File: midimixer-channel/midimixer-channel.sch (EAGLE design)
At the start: 115 parts, among them IC1 74LS595D, IC2 74LS595D, IC3 74LS595D, IC4 74165D, IC5 74165D, U1 LM1117IMPX-3.3/NOPB

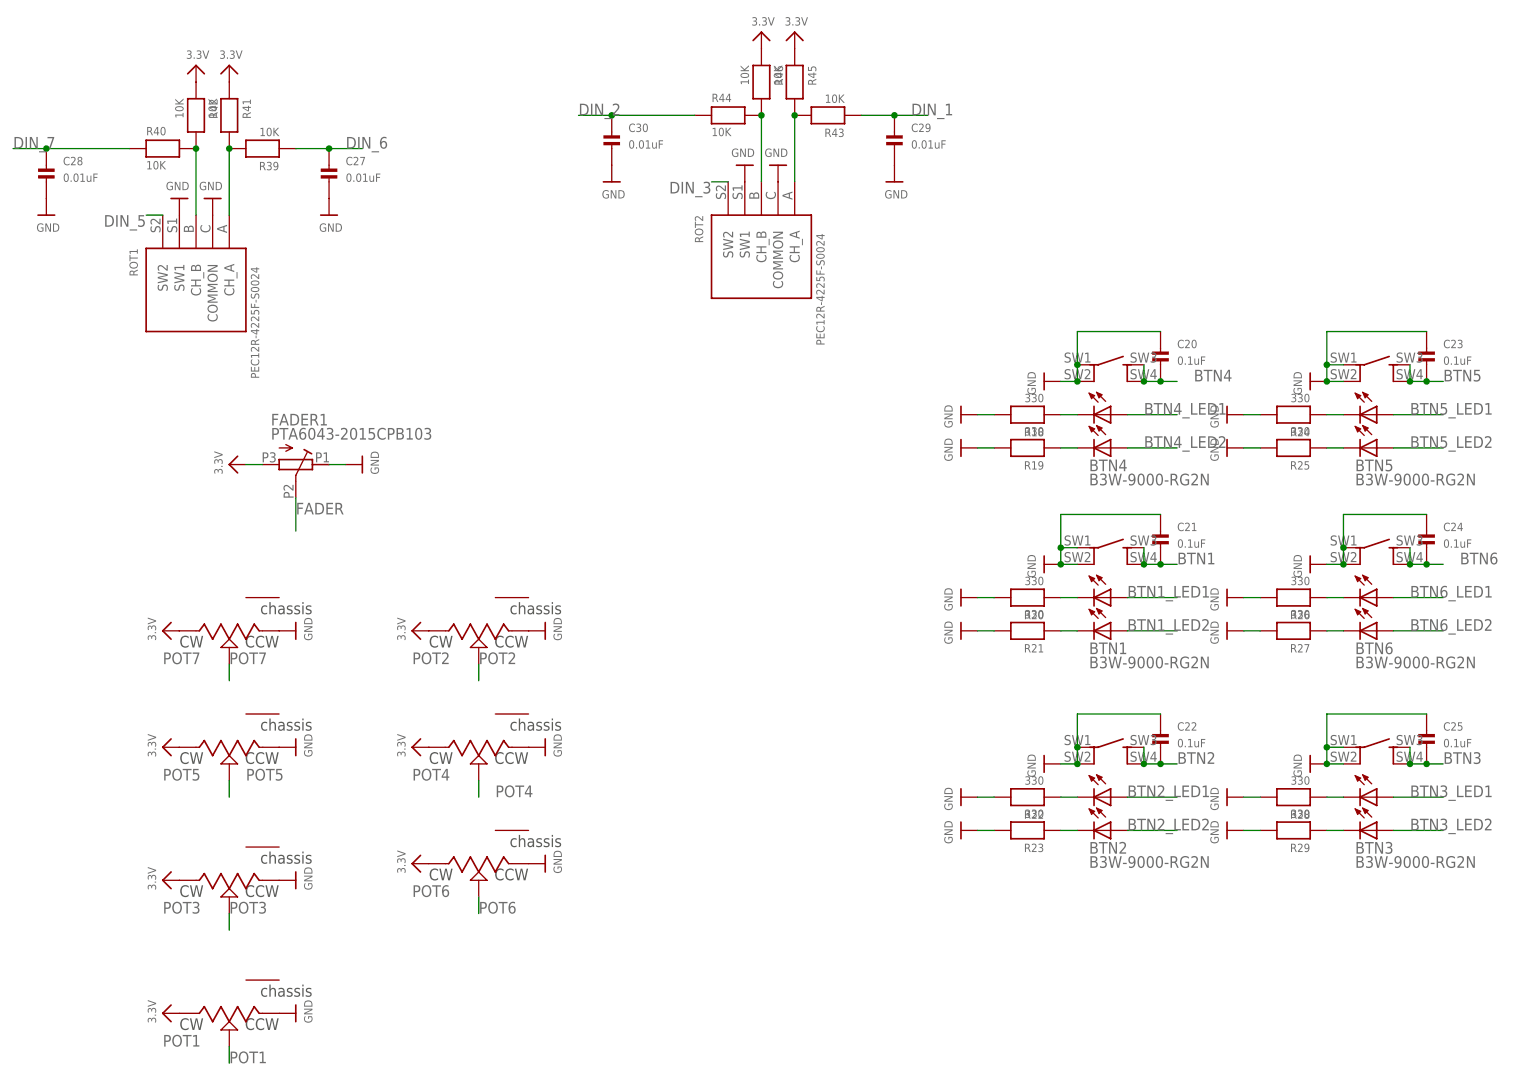
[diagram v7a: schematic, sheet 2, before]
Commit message: midimixer-channel: change green led resistors, some other misc changes
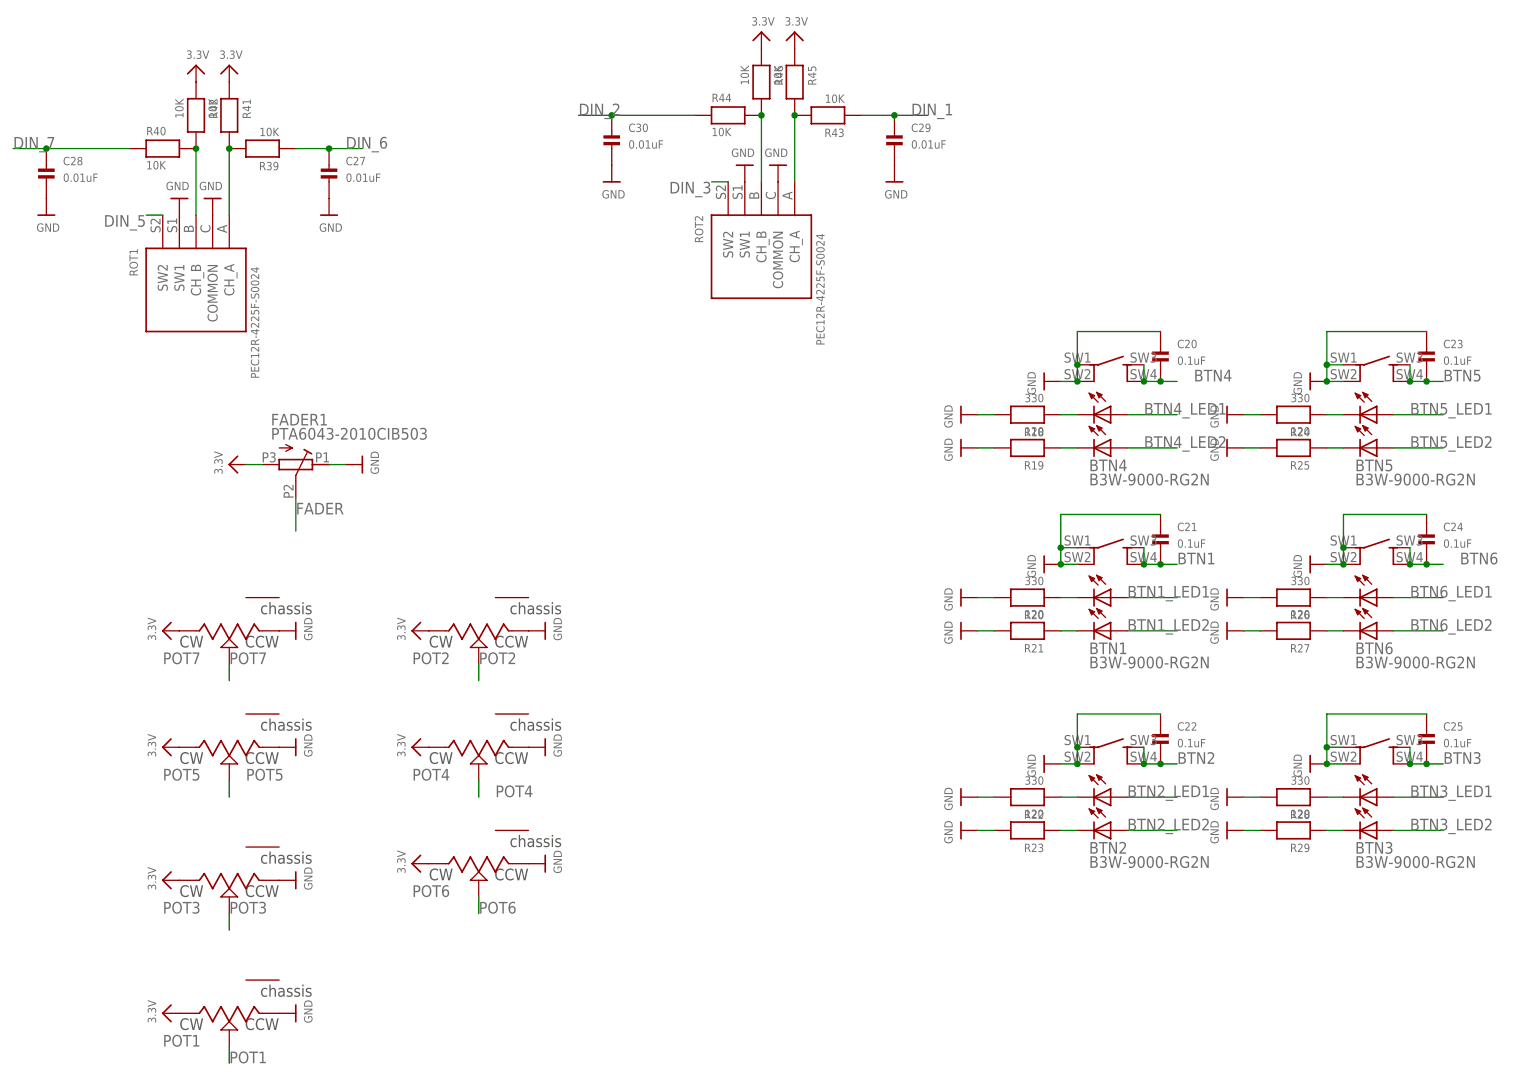
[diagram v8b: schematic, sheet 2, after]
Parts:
- FADER1: value PTA6043-2015CPB103 -> PTA6043-2010CIB503
- R19, R21, R23, R25, R27, R29: value 330 -> 120
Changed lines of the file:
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@@
 <part name="BTN4" library="keves" deviceset="B3W-9000-RG2N" device=""/>
 <part name="R18" library="microbuilder" deviceset="RESISTOR" device="0603" value="330"/>
-<part name="R19" library="microbuilder" deviceset="RESISTOR" device="0603" value="330"/>
+<part name="R19" library="microbuilder" deviceset="RESISTOR" device="0603" value="120"/>
 <part name="U$37" library="microbuilder" deviceset="GND" device=""/>
 <part name="U$38" library="microbuilder" deviceset="GND" device=""/>
@@
 <part name="U$40" library="microbuilder" deviceset="GND" device=""/>
 <part name="U$41" library="microbuilder" deviceset="GND" device=""/>
-<part name="FADER1" library="keves" deviceset="PTA6043-2015CPB103" device=""/>
+<part name="FADER1" library="keves" deviceset="PTA6043-2015CPB103" device="" value="PTA6043-2010CIB503"/>
 <part name="BTN1" library="keves" deviceset="B3W-9000-RG2N" device=""/>
 <part name="R20" library="microbuilder" deviceset="RESISTOR" device="0603" value="330"/>
-<part name="R21" library="microbuilder" deviceset="RESISTOR" device="0603" value="330"/>
+<part name="R21" library="microbuilder" deviceset="RESISTOR" device="0603" value="120"/>
 <part name="U$44" library="microbuilder" deviceset="GND" device=""/>
 <part name="U$45" library="microbuilder" deviceset="GND" device=""/>
@@
 <part name="BTN5" library="keves" deviceset="B3W-9000-RG2N" device=""/>
 <part name="R24" library="microbuilder" deviceset="RESISTOR" device="0603" value="330"/>
-<part name="R25" library="microbuilder" deviceset="RESISTOR" device="0603" value="330"/>
+<part name="R25" library="microbuilder" deviceset="RESISTOR" device="0603" value="120"/>
 <part name="U$48" library="microbuilder" deviceset="GND" device=""/>
 <part name="U$49" library="microbuilder" deviceset="GND" device=""/>
@@
 <part name="BTN6" library="keves" deviceset="B3W-9000-RG2N" device=""/>
 <part name="R26" library="microbuilder" deviceset="RESISTOR" device="0603" value="330"/>
-<part name="R27" library="microbuilder" deviceset="RESISTOR" device="0603" value="330"/>
+<part name="R27" library="microbuilder" deviceset="RESISTOR" device="0603" value="120"/>
 <part name="U$52" library="microbuilder" deviceset="GND" device=""/>
 <part name="U$53" library="microbuilder" deviceset="GND" device=""/>
@@
 <part name="BTN2" library="keves" deviceset="B3W-9000-RG2N" device=""/>
 <part name="R22" library="microbuilder" deviceset="RESISTOR" device="0603" value="330"/>
-<part name="R23" library="microbuilder" deviceset="RESISTOR" device="0603" value="330"/>
+<part name="R23" library="microbuilder" deviceset="RESISTOR" device="0603" value="120"/>
 <part name="U$56" library="microbuilder" deviceset="GND" device=""/>
 <part name="U$57" library="microbuilder" deviceset="GND" device=""/>
@@
 <part name="BTN3" library="keves" deviceset="B3W-9000-RG2N" device=""/>
 <part name="R28" library="microbuilder" deviceset="RESISTOR" device="0603" value="330"/>
-<part name="R29" library="microbuilder" deviceset="RESISTOR" device="0603" value="330"/>
+<part name="R29" library="microbuilder" deviceset="RESISTOR" device="0603" value="120"/>
 <part name="U$60" library="microbuilder" deviceset="GND" device=""/>
 <part name="U$61" library="microbuilder" deviceset="GND" device=""/>
